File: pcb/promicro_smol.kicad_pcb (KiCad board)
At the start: 2 copper layers, 15.2 x 33 mm, 31 parts, among them Q1 HL3134KT, Q2 HL3134KT, Q3 HL3134KT, Q4 HL3134KT, Q5 HL3134KT, U1 LSM6DSVTR, U2 QMC6309, U4 ProMicro NRF52840

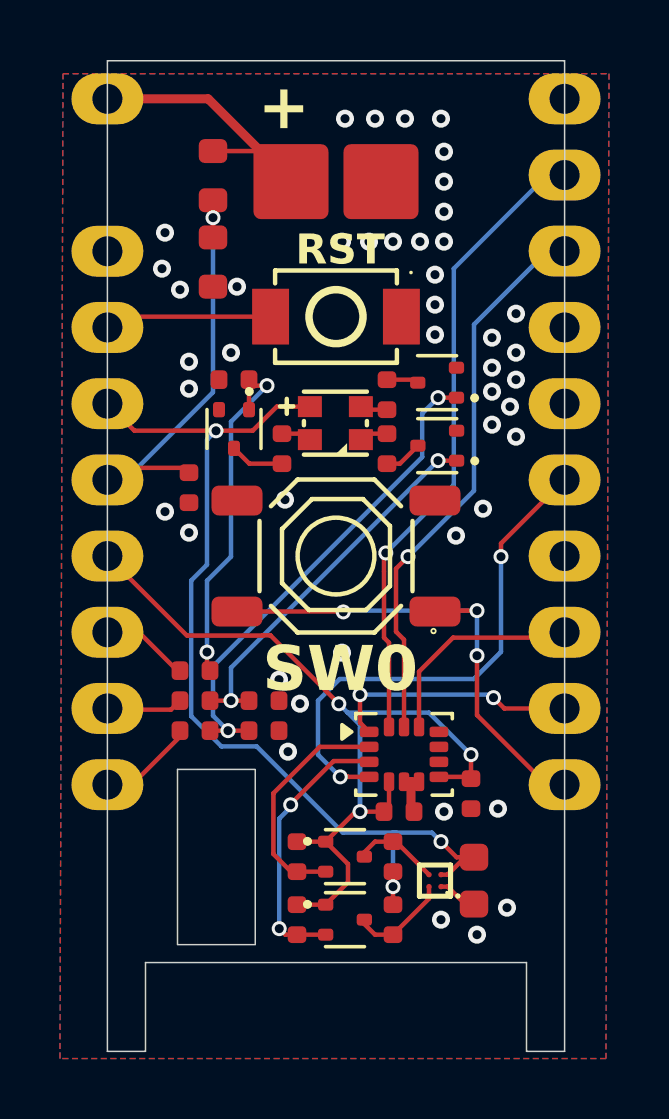
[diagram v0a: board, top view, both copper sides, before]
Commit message: feat: routing + ADC res
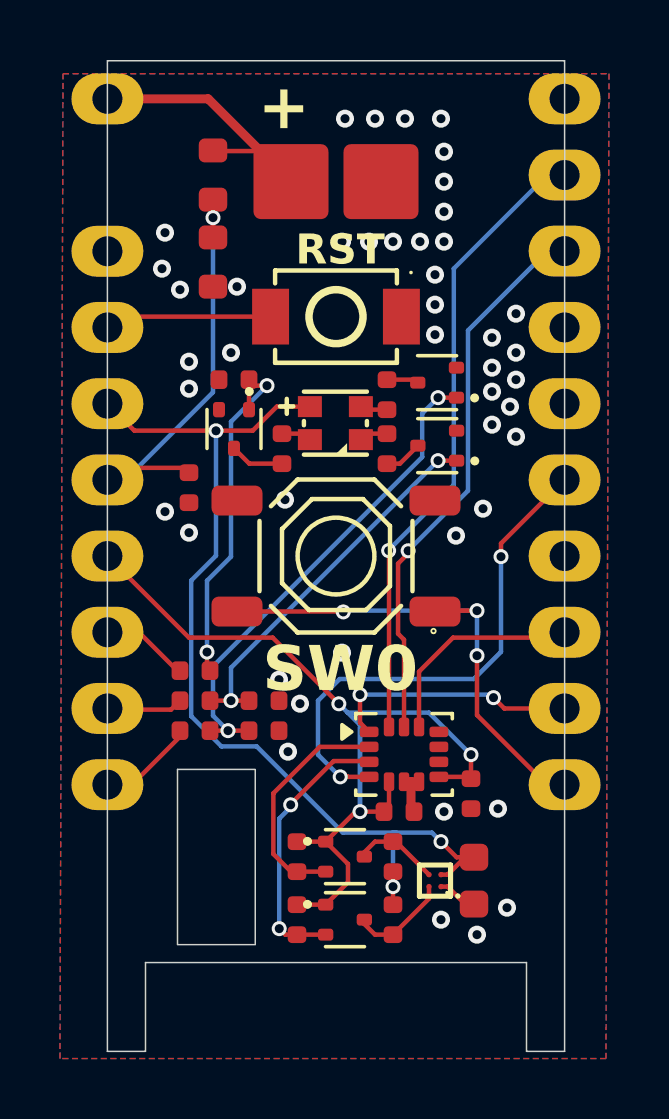
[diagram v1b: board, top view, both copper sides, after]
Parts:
- R11: value 4.7MΩ -> 5.1MΩ
